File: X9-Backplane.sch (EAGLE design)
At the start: 11 parts

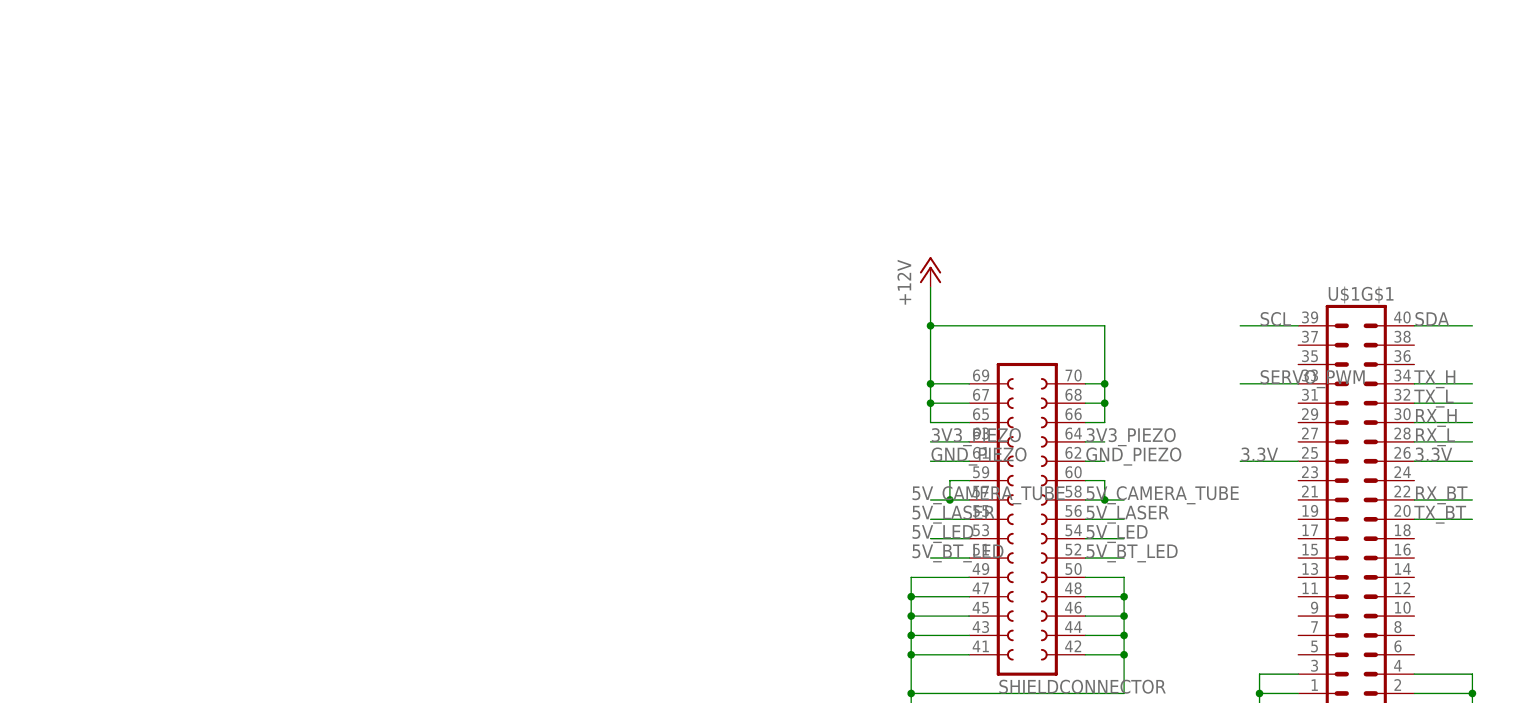
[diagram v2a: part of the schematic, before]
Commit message: added debugging pins
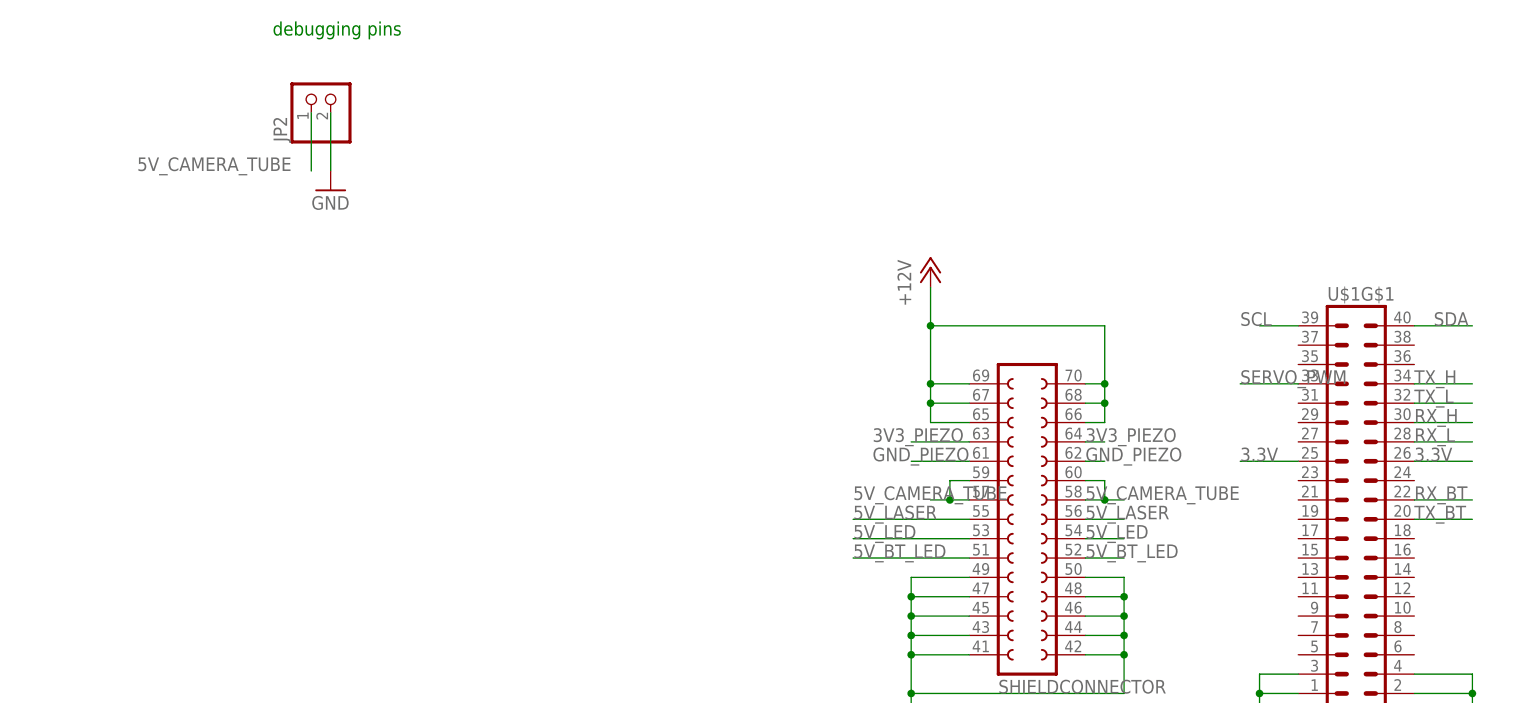
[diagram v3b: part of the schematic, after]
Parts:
- added JP2: (no value), pinhead:PINHD-1X2
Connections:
- net 5V_CAMERA_TUBE: now also JP2.1
- net GND: now also JP2.2
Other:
- note added: "debugging pins"
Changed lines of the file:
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@@
 <part name="FRAME2" library="frames" deviceset="FRAME_A_L" device=""/>
 <part name="FRAME3" library="frames" deviceset="FRAME_A_L" device=""/>
-<part name="FRAME4" library="frames" deviceset="FRAME_A_L" device=""/>
 <part name="POWER" library="T2I5P" deviceset="T2I5P" device=""/>
 <part name="CAMDATA" library="BACKPLANE" deviceset="T2I" device=""/>
@@
 <part name="GND2" library="supply1" deviceset="GND" device=""/>
 <part name="PS" library="con-hirose-df13" deviceset="DF13-4P-1.25" device="DSA"/>
+<part name="JP2" library="pinhead" deviceset="PINHD-1X2" device=""/>
+<part name="GND3" library="SparkFun-Aesthetics" deviceset="GND" device=""/>
 </parts>
 <sheets>
 <sheet>
 <plain>
+<text x="223.52" y="200.66" size="1.778" layer="91">debugging pins</text>
 </plain>
 <instances>
@@
 <instance part="FRAME3" gate="G$1" x="279.4" y="0"/>
 <instance part="FRAME3" gate="G$2" x="452.12" y="0"/>
-<instance part="FRAME4" gate="G$1" x="0" y="-215.9"/>
-<instance part="FRAME4" gate="G$2" x="172.72" y="-215.9"/>
 <instance part="POWER" gate="&gt;NAME" x="33.02" y="187.96"/>
 <instance part="CAMDATA" gate="G$1" x="33.02" y="114.3"/>
@@
 <attribute name="VALUE" x="61.9125" y="118.745" size="1.778" layer="96" rot="R270"/>
 </instance>
+<instance part="JP2" gate="G$1" x="231.14" y="193.04" rot="R90"/>
+<instance part="GND3" gate="1" x="231.14" y="180.34"/>
 </instances>
 <busses>
@@
 <segment>
 <pinref part="U$1" gate="G$2" pin="5V_LED@13"/>
-<wire x1="314.96" y1="134.62" x2="309.88" y2="134.62" width="0.1524" layer="91"/>
-<label x="307.34" y="134.62" size="1.778" layer="95"/>
+<wire x1="314.96" y1="134.62" x2="299.72" y2="134.62" width="0.1524" layer="91"/>
+<label x="299.72" y="134.62" size="1.778" layer="95"/>
 </segment>
 </net>
@@
 <label x="68.58" y="73.66" size="1.778" layer="95" rot="R90"/>
 </segment>
+<segment>
+<pinref part="JP2" gate="G$1" pin="2"/>
+<wire x1="231.14" y1="190.5" x2="231.14" y2="182.88" width="0.1524" layer="91"/>
+<pinref part="GND3" gate="1" pin="GND"/>
+</segment>
 </net>
 <net name="TX_H" class="0">
@@
 <segment>
 <pinref part="U$1" gate="G$2" pin="3V3_PIEZO@23"/>
-<wire x1="314.96" y1="147.32" x2="309.88" y2="147.32" width="0.1524" layer="91"/>
-<label x="309.88" y="147.32" size="1.778" layer="95"/>
+<wire x1="314.96" y1="147.32" x2="307.34" y2="147.32" width="0.1524" layer="91"/>
+<label x="302.26" y="147.32" size="1.778" layer="95"/>
 </segment>
 <segment>
@@
 <segment>
 <pinref part="U$1" gate="G$1" pin="SCL@39"/>
-<wire x1="358.14" y1="162.56" x2="350.52" y2="162.56" width="0.1524" layer="91"/>
-<label x="353.06" y="162.56" size="1.778" layer="95"/>
+<wire x1="358.14" y1="162.56" x2="353.06" y2="162.56" width="0.1524" layer="91"/>
+<label x="350.52" y="162.56" size="1.778" layer="95"/>
 </segment>
 <segment>
@@
 <pinref part="U$1" gate="G$1" pin="SDA@40"/>
 <wire x1="373.38" y1="162.56" x2="381" y2="162.56" width="0.1524" layer="91"/>
-<label x="373.38" y="162.56" size="1.778" layer="95"/>
+<label x="375.92" y="162.56" size="1.778" layer="95"/>
 </segment>
 <segment>
@@
 <segment>
 <pinref part="U$1" gate="G$2" pin="5V_LASER@15"/>
-<wire x1="314.96" y1="137.16" x2="309.88" y2="137.16" width="0.1524" layer="91"/>
-<label x="307.34" y="137.16" size="1.778" layer="95"/>
+<wire x1="314.96" y1="137.16" x2="299.72" y2="137.16" width="0.1524" layer="91"/>
+<label x="299.72" y="137.16" size="1.778" layer="95"/>
 </segment>
 </net>
@@
 <segment>
 <pinref part="U$1" gate="G$2" pin="GND_PIEZO@21"/>
-<wire x1="314.96" y1="144.78" x2="309.88" y2="144.78" width="0.1524" layer="91"/>
-<label x="309.88" y="144.78" size="1.778" layer="95"/>
+<wire x1="314.96" y1="144.78" x2="307.34" y2="144.78" width="0.1524" layer="91"/>
+<label x="302.26" y="144.78" size="1.778" layer="95"/>
 </segment>
 <segment>
@@
 <pinref part="U$1" gate="G$1" pin="SERVO_PWM@33"/>
 <wire x1="358.14" y1="154.94" x2="350.52" y2="154.94" width="0.1524" layer="91"/>
-<label x="353.06" y="154.94" size="1.778" layer="95"/>
+<label x="350.52" y="154.94" size="1.778" layer="95"/>
 </segment>
 <segment>
@@
 <wire x1="312.42" y1="142.24" x2="312.42" y2="139.7" width="0.1524" layer="91"/>
 <junction x="312.42" y="139.7"/>
-<label x="307.34" y="139.7" size="1.778" layer="95"/>
+<label x="299.72" y="139.7" size="1.778" layer="95"/>
 </segment>
 <segment>
@@
 <label x="35.56" y="106.68" size="1.778" layer="95" rot="R90"/>
 </segment>
+<segment>
+<pinref part="JP2" gate="G$1" pin="1"/>
+<wire x1="228.6" y1="190.5" x2="228.6" y2="182.88" width="0.1524" layer="91"/>
+<label x="205.74" y="182.88" size="1.778" layer="95"/>
+</segment>
 </net>
 <net name="5V_BT_LED" class="0">
@@
 <segment>
 <pinref part="U$1" gate="G$2" pin="5V_BT_LED@11"/>
-<wire x1="314.96" y1="132.08" x2="309.88" y2="132.08" width="0.1524" layer="91"/>
-<label x="307.34" y="132.08" size="1.778" layer="95"/>
-</segment>
-<segment>
+<wire x1="314.96" y1="132.08" x2="299.72" y2="132.08" width="0.1524" layer="91"/>
+<label x="299.72" y="132.08" size="1.778" layer="95"/>
+</segment>
+<segment>

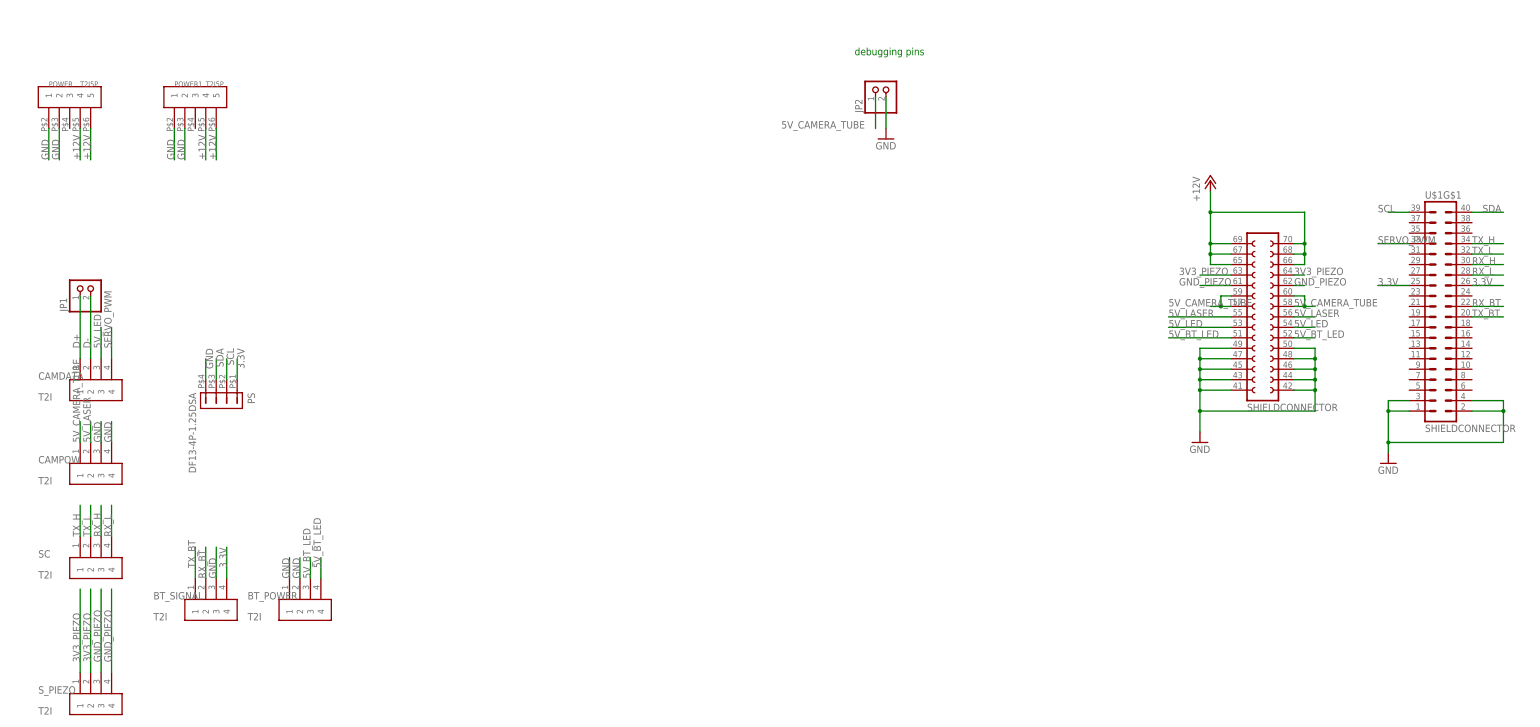
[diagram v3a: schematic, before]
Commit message: reordered where the binders will be placed
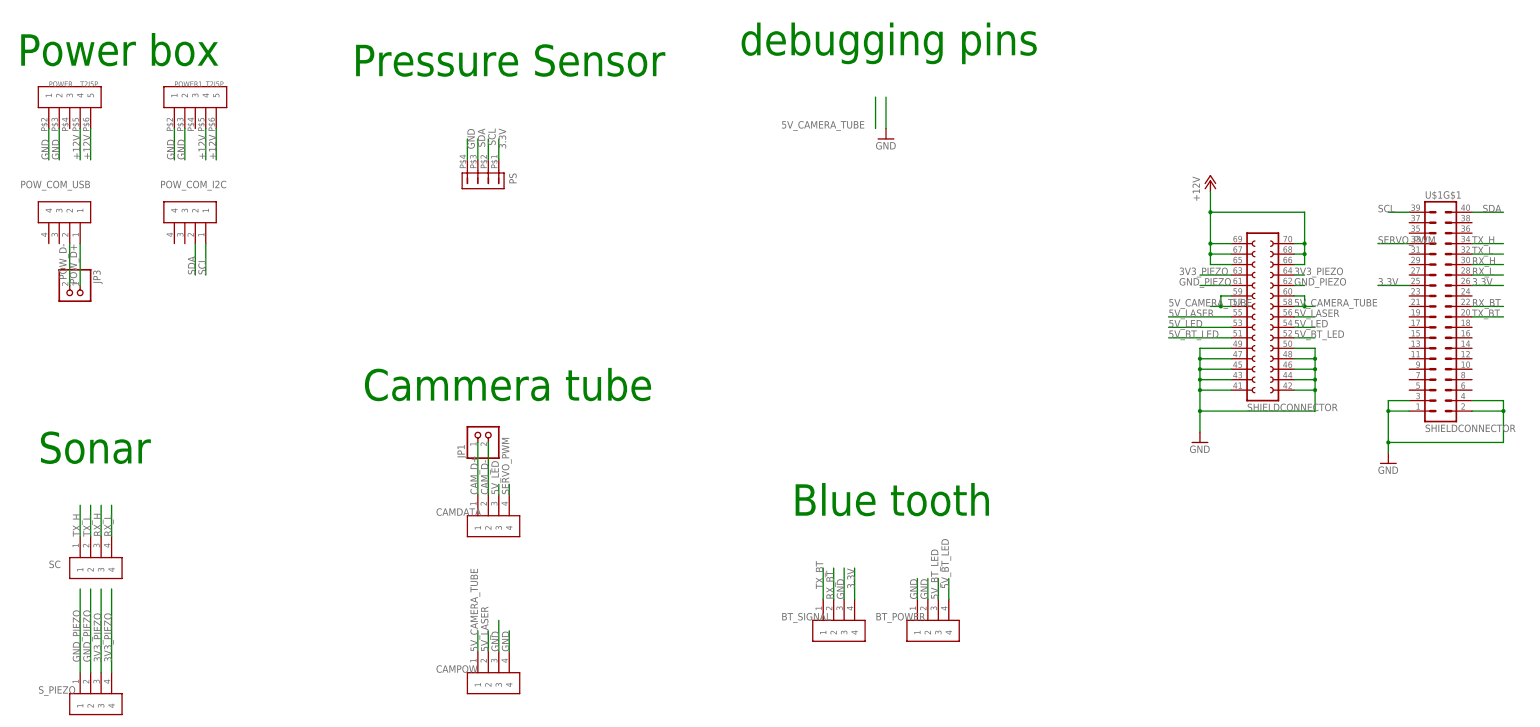
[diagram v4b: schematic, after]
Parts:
- removed JP2: (no value), pinhead:PINHD-1X2
- added JP3: (no value), pinhead:PINHD-1X2
- added POW_COM_I2C, POW_COM_USB: T2I, BACKPLANE:T2I
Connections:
- net D+ renamed CAM_D+
- net D- renamed CAM_D-
- new net POW_D+: JP3.1, POW_COM_USB.1
- new net POW_D-: JP3.2, POW_COM_USB.2
- net 3V3_PIEZO: now also S_PIEZO.3, S_PIEZO.4; no longer S_PIEZO.1, S_PIEZO.2
- net 5V_CAMERA_TUBE: no longer JP2.1
- net GND: no longer JP2.2
- net GND_PIEZO: now also S_PIEZO.1, S_PIEZO.2; no longer S_PIEZO.3, S_PIEZO.4
- net SCL: now also POW_COM_I2C.1
- net SDA: now also POW_COM_I2C.2
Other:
- note added: "Blue tooth"
- note added: "Cammera tube"
- note added: "Power box"
- note added: "Pressure Sensor"
- note added: "Sonar"
- moved on the sheet: BT_POWER, BT_SIGNAL, CAMDATA, CAMPOW, JP1, PS

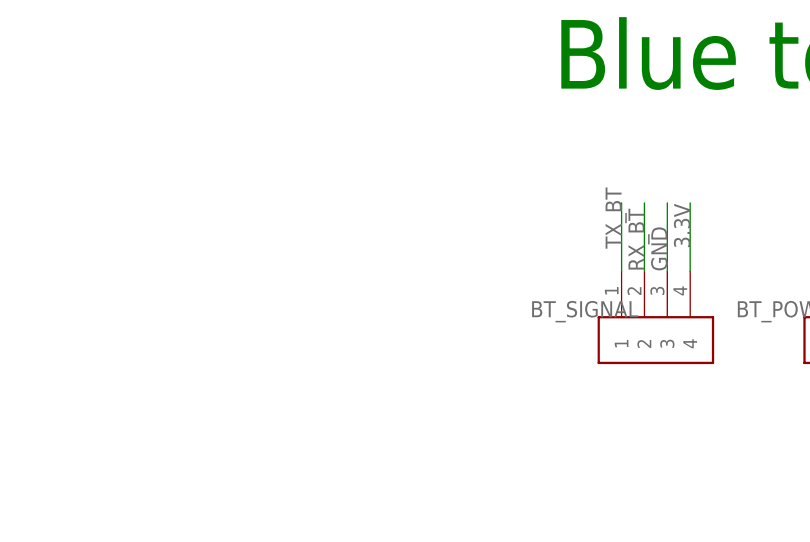
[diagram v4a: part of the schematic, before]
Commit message: Added extra connector for bluetooth just in case
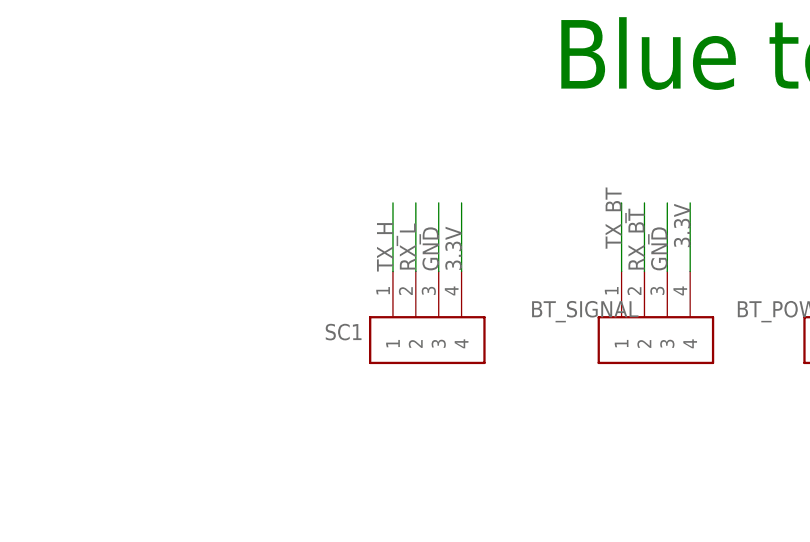
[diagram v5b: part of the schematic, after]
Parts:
- added SC1: T2I, BACKPLANE:T2I
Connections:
- net 3.3V: now also SC1.4
- net GND: now also SC1.3
- net RX_L: now also SC1.2
- net TX_H: now also SC1.1
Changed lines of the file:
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@@
 <part name="JP3" library="pinhead" deviceset="PINHD-1X2" device=""/>
 <part name="POW_COM_I2C" library="BACKPLANE" deviceset="T2I" device=""/>
+<part name="SC1" library="BACKPLANE" deviceset="T2I" device=""/>
 </parts>
 <sheets>
@@
 <attribute name="NAME" x="71.12" y="170.18" size="1.778" layer="95" rot="R180"/>
 </instance>
+<instance part="SC1" gate="G$1" x="187.96" y="55.88" smashed="yes">
+<attribute name="NAME" x="182.88" y="60.96" size="1.778" layer="95"/>
+</instance>
 </instances>
 <busses>
@@
 <wire x1="223.52" y1="68.58" x2="223.52" y2="76.2" width="0.1524" layer="91"/>
 <label x="223.52" y="71.12" size="1.778" layer="95" rot="R90"/>
+</segment>
+<segment>
+<pinref part="SC1" gate="G$1" pin="4"/>
+<wire x1="198.12" y1="68.58" x2="198.12" y2="76.2" width="0.1524" layer="91"/>
+<label x="198.12" y="68.58" size="1.778" layer="95" rot="R90"/>
 </segment>
 </net>
@@
 <pinref part="GND3" gate="1" pin="GND"/>
 </segment>
+<segment>
+<pinref part="SC1" gate="G$1" pin="3"/>
+<wire x1="195.58" y1="68.58" x2="195.58" y2="76.2" width="0.1524" layer="91"/>
+<label x="195.58" y="68.58" size="1.778" layer="95" rot="R90"/>
+</segment>
 </net>
 <net name="TX_H" class="0">
@@
 <label x="373.38" y="154.94" size="1.778" layer="95"/>
 </segment>
+<segment>
+<pinref part="SC1" gate="G$1" pin="1"/>
+<wire x1="190.5" y1="68.58" x2="190.5" y2="76.2" width="0.1524" layer="91"/>
+<label x="190.5" y="68.58" size="1.778" layer="95" rot="R90"/>
+</segment>
 </net>
 <net name="3V3_PIEZO" class="0">
@@
 <label x="373.38" y="147.32" size="1.778" layer="95"/>
 </segment>
-</net>
+<segment>
+<pinref part="SC1" gate="G$1" pin="2"/>
+<wire x1="193.04" y1="68.58" x2="193.04" y2="76.2" width="0.1524" layer="91"/>
+<label x="193.04" y="68.58" size="1.778" layer="95" rot="R90"/>
+</segment>
+</net>
